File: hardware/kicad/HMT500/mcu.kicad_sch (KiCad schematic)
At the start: 19 parts, among them J2 TC2030-IDC-NL, U4 STM32L431RCT6

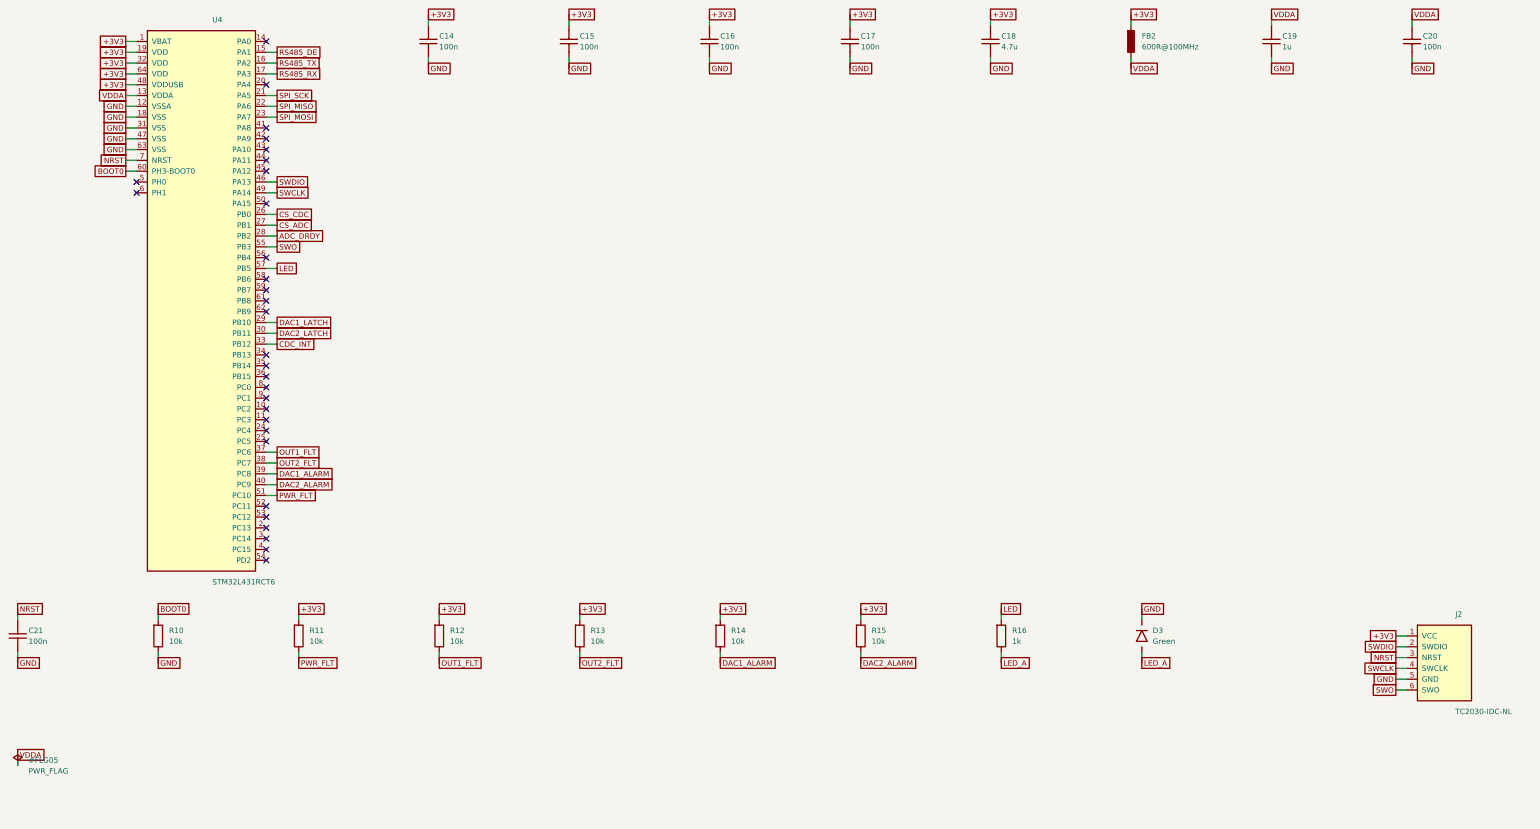
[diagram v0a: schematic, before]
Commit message: KiCad schematic v0.2: hand-laid-out, wired, readable sheets with power symbols and functional blocks
Replaces the label-only v0.1. Drawing rules are validated at generation and
the drawn netlist is checked against design intent (71 nets, 0 errors).

Co-Authored-By: Claude Opus 5.5 <noreply@anthropic.com>
Claude-Session: https://claude.ai/code/session_01JA2o8uJsqp9Vzsg4b665ev
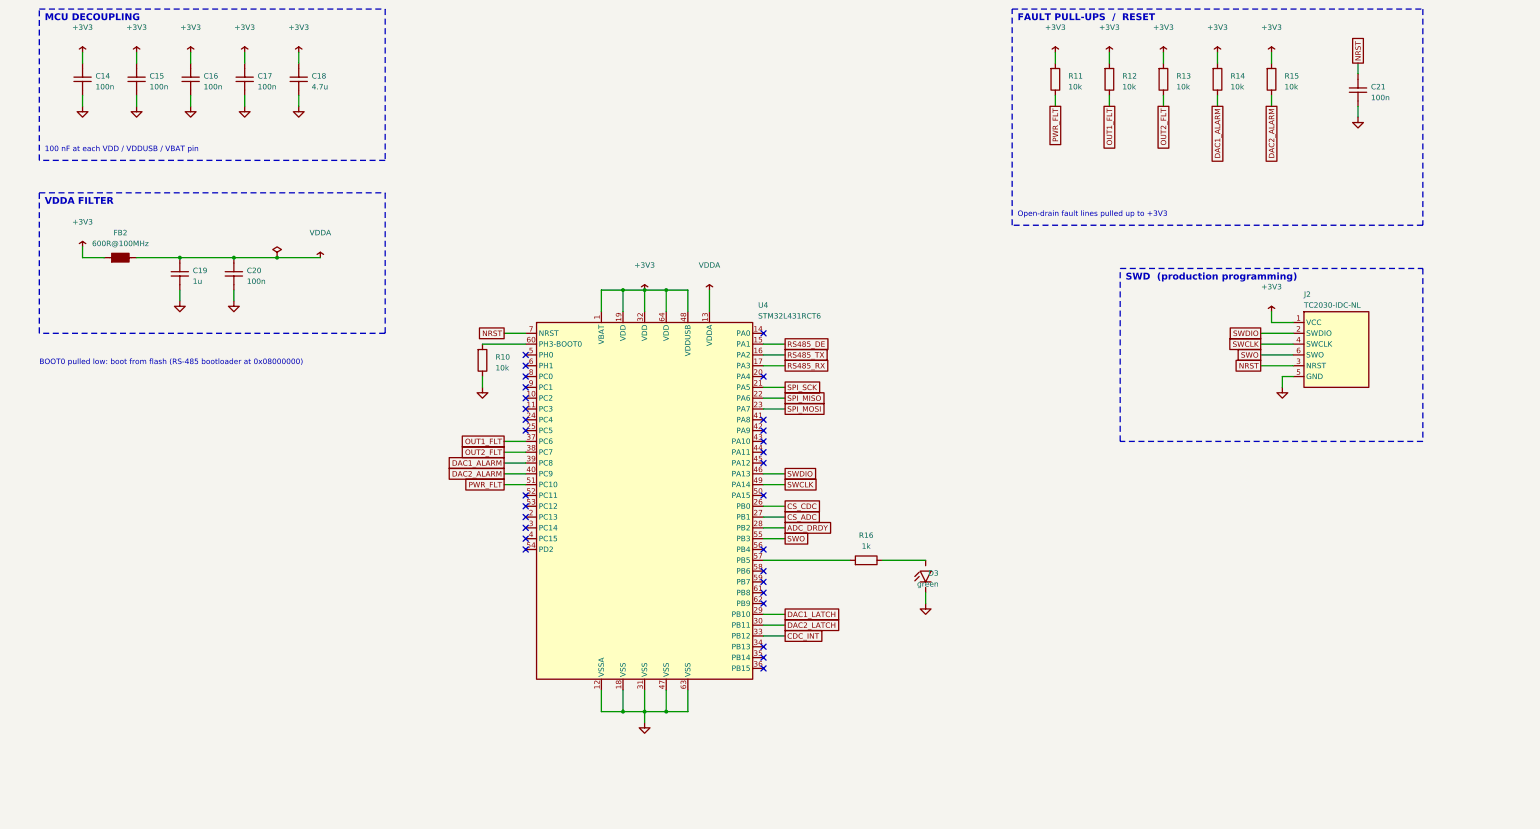
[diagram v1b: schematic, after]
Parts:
- D3: value Green -> green
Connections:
- net BOOT0: no longer names the net of R10.1, U4.60 (PH3-BOOT0)
- net LED: no longer names the net of R16.1, U4.57 (PB5)
- net LED_A: no longer names the net of D3.2, R16.2
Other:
- note added: "100 nF at each VDD / VDDUSB / VBAT pin"
- note added: "BOOT0 pulled low: boot from flash (RS-485 bootloader at 0x08000000)"
- note added: "FAULT PULL-UPS / RESET"
- note added: "MCU DECOUPLING"
- note added: "Open-drain fault lines pulled up to +3V3"
- note added: "SWD (production programming)"
- note added: "VDDA FILTER"
- title: HMT500 - MCU STM32L431, SWD, status LED -> HMT500  MCU
- moved on the sheet: C14, C15, C16, C17, C18, C19, C20, C21, J2, R10, R11, R12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

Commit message: Switch MCU to STM32G0B1CCT3 (in-house part, 125 C grade)
DOTECH already uses the STM32G0B1CCT6 in DP2000. Use the -40..125 C
grade of the same chip so tooling, drivers and production fixtures
can be shared.

- Schematic: new LQFP48 symbol with pin numbers from the official
  KiCad STM32G0B1C_B-C-E_Tx symbol. NRST is on PF2. BOOT0 shares
  PA14/SWCLK, so the pull-down is removed and the option bytes select
  flash boot. SWO is gone (Cortex-M0+), so J2 pin 6 is NC. VREF+ is
  fed from the FB2 filter. Faults and alarms move to PB13-15. The
  netlist check passes: 69 nets, 0 errors.
- Pin table, block design, BOM and cost updated. The bootloader doc
  now covers G0B1 dual-bank page erase, the prefetch erratum and the
  option bytes.
- Mech: MCU footprint in the 3D and drawings is now 7x7. STEP files,
  renders and the KiCad board regenerated.
- MCU review: fix product names read from the purchase report
  (HPX3000, HTP1100W) and mark the decision.

Co-Authored-By: Claude Opus 5.5 <noreply@anthropic.com>
Claude-Session: https://claude.ai/code/session_01JA2o8uJsqp9Vzsg4b665ev
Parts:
- removed C16, C17: 100n, Capacitor_SMD:C_0603_1608Metric, symbol HMT500:C
- removed R10: 10k, Resistor_SMD:R_0603_1608Metric, symbol HMT500:R
- U4: value STM32L431RCT6 -> STM32G0B1CCT3; footprint Package_QFP:LQFP-64_10x10mm_P0.5mm -> Package_QFP:LQFP-48_7x7mm_P0.5mm; symbol HMT500:STM32L431RCTx -> HMT500:STM32G0B1CxTx
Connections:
- net +3V3: now also U4.4 (VBAT), U4.6 (VDD); no longer U4.1 (VBAT), U4.19 (VDD), U4.32 (VDD), U4.48 (VDDUSB), U4.64 (VDD)
- net ADC_DRDY: now also U4.21 (PB2); no longer U4.28 (PB2)
- net CDC_INT: now also U4.24 (PB12); no longer U4.33 (PB12)
- net CS_ADC: now also U4.20 (PB1); no longer U4.27 (PB1)
- net CS_CDC: now also U4.19 (PB0); no longer U4.26 (PB0)
- net DAC1_ALARM: now also U4.25 (PB13); no longer U4.39 (PC8)
- net DAC1_LATCH: now also U4.22 (PB10); no longer U4.29 (PB10)
- net DAC2_ALARM: now also U4.26 (PB14); no longer U4.40 (PC9)
- net DAC2_LATCH: now also U4.23 (PB11); no longer U4.30 (PB11)
- net GND: now also U4.7 (VSS); no longer U4.12 (VSSA), U4.18 (VSS), U4.31 (VSS), U4.47 (VSS), U4.63 (VSS)
- net NRST: now also U4.10 (PF2-NRST); no longer U4.7 (NRST)
- net OUT1_FLT: now also U4.30 (PC6); no longer U4.37 (PC6)
- net OUT2_FLT: now also U4.31 (PC7); no longer U4.38 (PC7)
- net PWR_FLT: now also U4.27 (PB15); no longer U4.51 (PC10)
- net RS485_DE: now also U4.12 (PA1); no longer U4.15 (PA1)
- net RS485_RX: now also U4.14 (PA3); no longer U4.17 (PA3)
- net RS485_TX: now also U4.13 (PA2); no longer U4.16 (PA2)
- net SPI_MISO: now also U4.17 (PA6); no longer U4.22 (PA6)
- net SPI_MOSI: now also U4.18 (PA7); no longer U4.23 (PA7)
- net SPI_SCK: now also U4.16 (PA5); no longer U4.21 (PA5)
- net SWCLK: now also U4.36 (PA14-BOOT0); no longer U4.49 (PA14)
- net SWDIO: now also U4.35 (PA13); no longer U4.46 (PA13)
- net VDDA: now also U4.5 (VREF+); no longer U4.13 (VDDA)
- net at U4.44 (PB5): now also R16.1
- net SWO: no longer names the net of J2.6 (SWO)
- net SWO: no longer U4.55 (PB3)
- no-connect marks 30 -> 24
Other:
- note added: "-> boot from flash (RS-485 bootloader 0x08000000)."
- note added: "100 nF at VDD and VBAT, 4.7 uF bulk"
- note added: "BOOT0 shares PA14/SWCLK - no pull-down."
- note added: "Cortex-M0+: no SWO (J2 pin 6 NC)."
- note added: "MCU NOTES (STM32G0B1)"
- note added: "Option bytes: nBOOT_SEL=1, nBOOT0=1"
- note added: "Same die as DP2000 (G0B1CCT6); T3 = -40..125 C."
- note added: "VDDA bonded to VDD in LQFP48; VREF+ via FB2."
- note removed: "100 nF at each VDD / VDDUSB / VBAT pin"
- note removed: "BOOT0 pulled low: boot from flash (RS-485 bootloader at 0x08000000)"
- moved on the sheet: C18

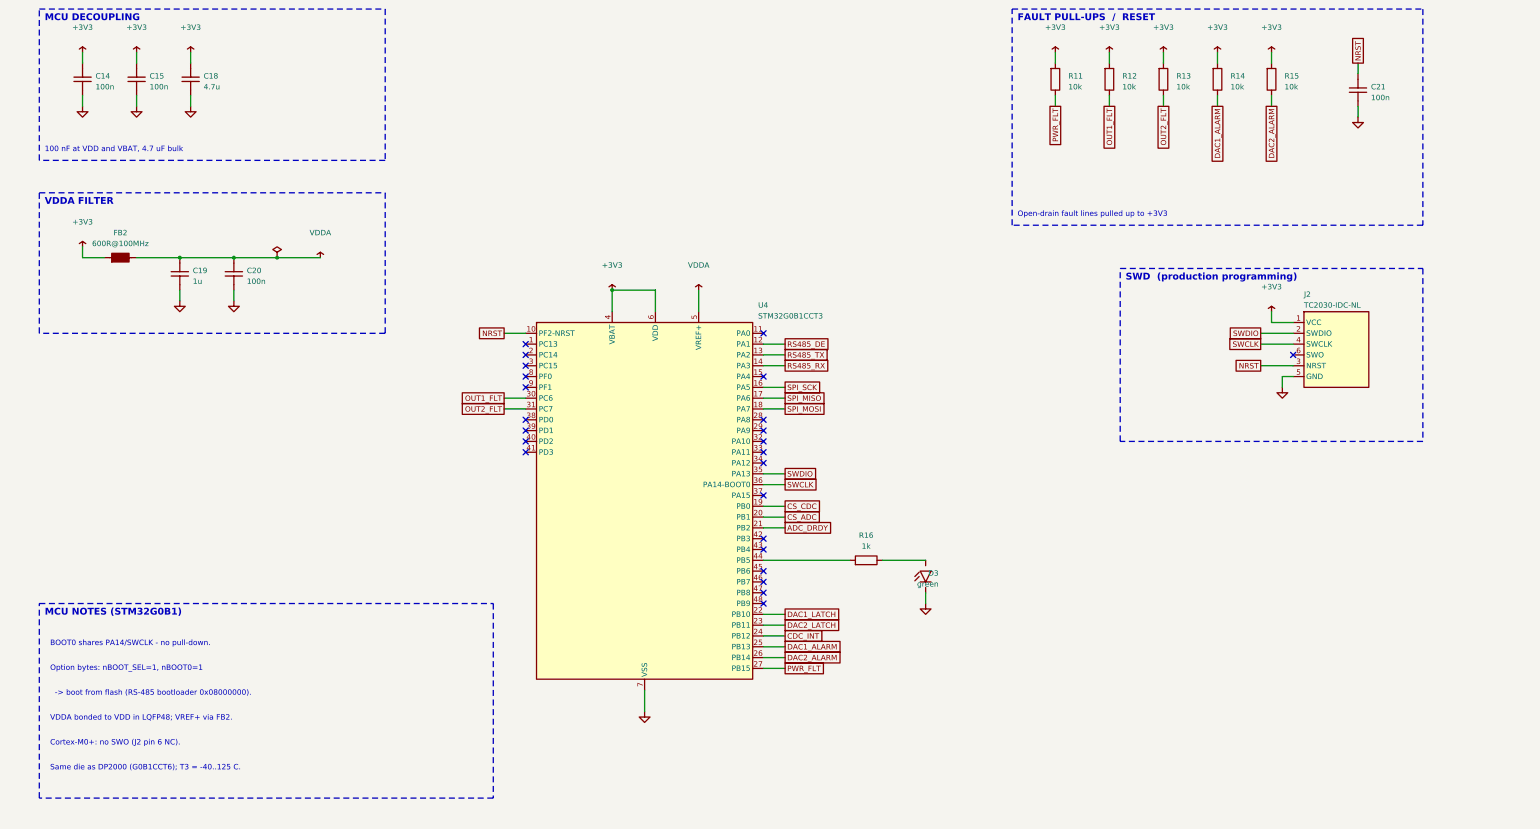
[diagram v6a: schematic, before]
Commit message: Schematic drawing rules: no overlapping text, Korean font, distinct net names
- Generator places reference/value text automatically, clear of symbol bodies,
  pins, wires, labels, notes and box edges; validation fails on any overlap
  (also note text vs wires/power names and bodies vs box edges)
- Fix 180-degree parts (LED) whose justification KiCad mirrors
- Styles: reference bold, value normal, power nets italic, signal nets boxed labels
- Korean box subtitles and legend in NanumGothic TrueType (stroke font has no Hangul)
- Nets renamed where they matched part or pin names: LED -> STAT_LED, EF_ILIM/IMON/DVDT
- J1 GH mounting pads removed from the symbol (PCB only); connector sheet re-spaced
- Schematic PDF export added; tests for net naming and Hangul font

Co-Authored-By: Claude Opus 5.5 <noreply@anthropic.com>
Claude-Session: https://claude.ai/code/session_01JA2o8uJsqp9Vzsg4b665ev
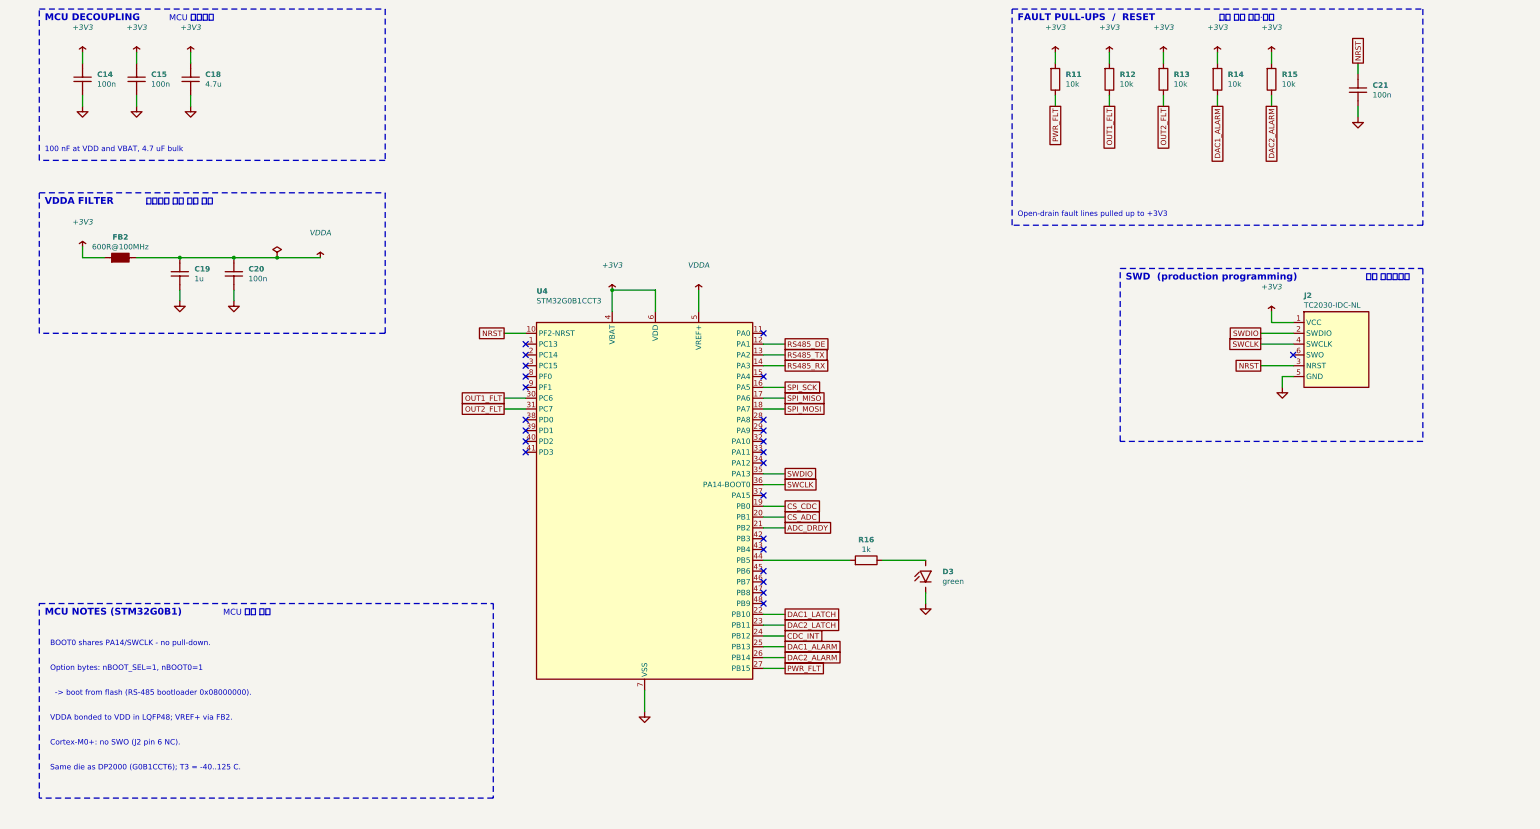
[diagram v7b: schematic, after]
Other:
- note added: "MCU 바이패스"
- note added: "MCU 설정 메모"
- note added: "고장 신호 풀업·리셋"
- note added: "생산 프로그래밍"
- note added: "아날로그 기준 전원 필터"

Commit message: Schematic v0.6: parts cleanup (91 -> 75) and PCB temperature sensing
- Removed: fault pull-ups R11-R15 (MCU internal pull-ups), status LED D3/R16
  (not visible after potting), RS-485 R60/R61/D60/D61 (THVD2450 built-in
  protection), VREF+ filter FB2/C19 (MCU ADC only for diagnostics), C11/C2/C6
  (duplicated by adjacent capacitors); VREF+ tied to +3V3 with C20
- PCB temperature with no added parts: ADS1220 internal sensor at the measurement
  front, STM32G0 internal sensor mid-board; compensation plan in circuit-design 5B
- 63 nets, netlist check 0 errors; parts list regenerated; decision log #22/#23

Co-Authored-By: Claude Opus 5.5 <noreply@anthropic.com>
Claude-Session: https://claude.ai/code/session_01JA2o8uJsqp9Vzsg4b665ev
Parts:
- removed C19: 1u, Capacitor_SMD:C_0603_1608Metric, symbol HMT500:C
- removed D3: green, LED_SMD:LED_0603_1608Metric, symbol HMT500:LED
- removed FB2: 600R@100MHz, Inductor_SMD:L_0603_1608Metric, symbol HMT500:FB
- removed R11, R12, R13, R14, R15: 10k, Resistor_SMD:R_0603_1608Metric, symbol HMT500:R
- removed R16: 1k, Resistor_SMD:R_0603_1608Metric, symbol HMT500:R
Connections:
- net VDDA is gone; now on net +3V3: C20.1, U4.5 (VREF+)
- no-connect marks 24 -> 25
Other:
- note added: "(PB13-15, PC6-7 internal)"
- note added: "100 nF at VDD, VBAT, VREF+ (C20); 4.7 uF bulk"
- note added: "Fault lines: MCU pull-ups"
- note added: "PCB temp (mid): internal sensor, ADC ch TS + TS_CAL."
- note added: "RESET"
- note added: "VDDA = VDD (LQFP48); VREF+ tied to +3V3 (C20)."
- note added: "리셋"
- note removed: "100 nF at VDD and VBAT, 4.7 uF bulk"
- note removed: "FAULT PULL-UPS / RESET"
- note removed: "Open-drain fault lines pulled up to +3V3"
- note removed: "VDDA FILTER"
- note removed: "VDDA bonded to VDD in LQFP48; VREF+ via FB2."
- note removed: "고장 신호 풀업·리셋"
- note removed: "아날로그 기준 전원 필터"
- moved on the sheet: C18, C20
